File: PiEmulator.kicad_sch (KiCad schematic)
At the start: 26 parts, among them J1 Conn_01x01, J2 Conn_01x01, J3 USB_C_Receptacle_USB2.0, U1 ADA3708, U3 BQ24090DGQ

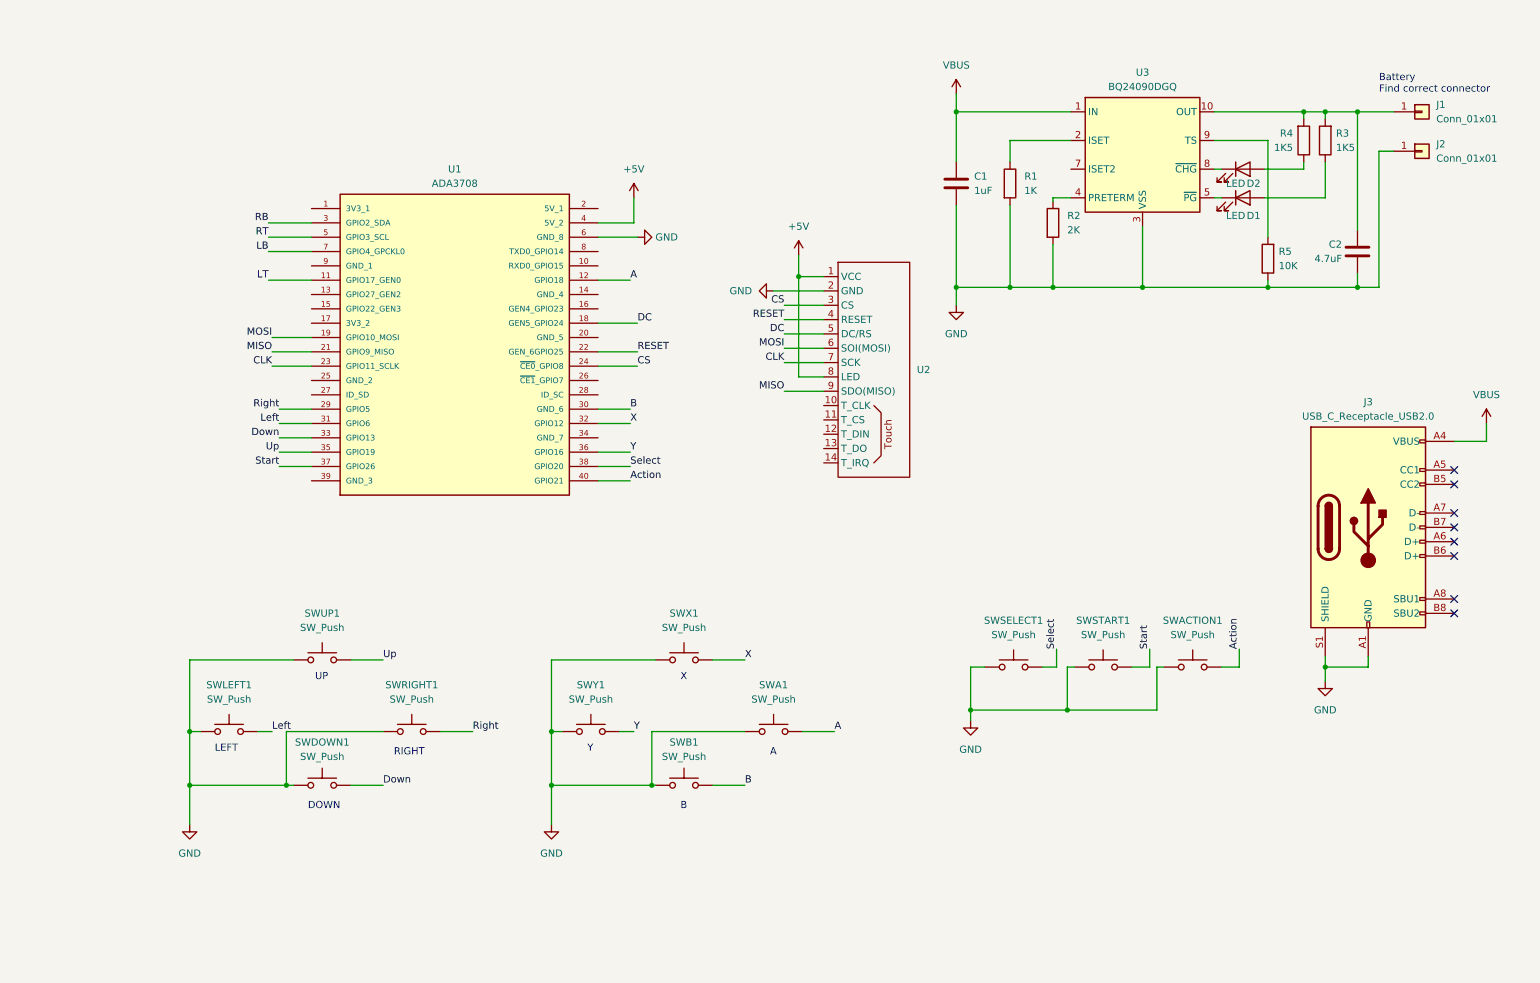
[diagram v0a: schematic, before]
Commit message: swapped buttons
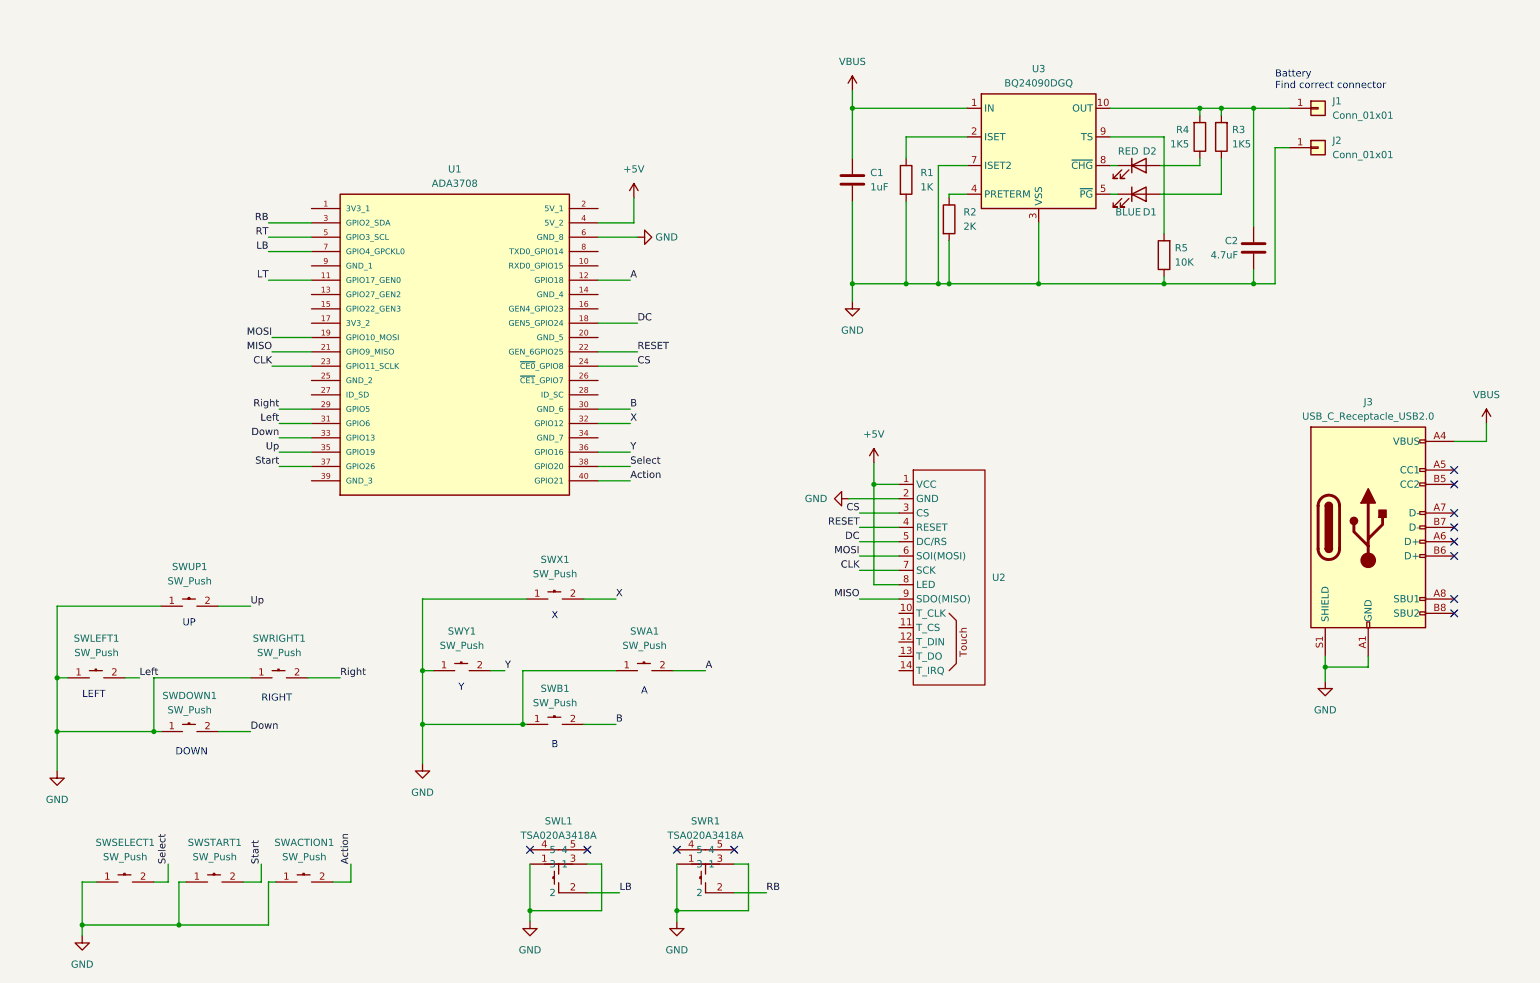
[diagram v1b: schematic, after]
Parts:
- removed SWA1, SWACTION1, SWB1, SWDOWN1, SWLEFT1, SWRIGHT1, SWSELECT1, SWSTART1, SWUP1, SWX1, SWY1: SW_Push, Button_Switch_SMD:PCB-Button, symbol Switch:SW_Push
- added SWA1, SWACTION1, SWB1, SWDOWN1, SWLEFT1, SWRIGHT1, SWSELECT1, SWSTART1, SWUP1, SWX1, SWY1: SW_Push, easyeda2kicad:SW-SMD_4P-L6.2-W6.2-P4.00-LS7.0, symbol easyeda2kicad:GT-TC063F-H025-L30
- added SWL1, SWR1: TSA020A3418A, easyeda2kicad:SW-SMD_TSA020XXXXXX, symbol easyeda2kicad:TSA020A3418A
- D1: value LED -> BLUE
- D2: value LED -> RED
- J1: footprint (none) -> Connector_Wago:SolderWirePad_4x4mm
- J2: footprint (none) -> Connector_Wire:Solder_Pad_4x4mm
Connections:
- net A: now also SWA1.2
- net Action: now also SWACTION1.2
- net B: now also SWB1.2
- net Down: now also SWDOWN1.2
- net GND: now also U3.7 (ISET2), SWA1.1, SWACTION1.1, SWB1.1, SWDOWN1.1, SWL1.1, SWL1.3, SWLEFT1.1, SWR1.1, SWR1.3, SWRIGHT1.1, SWSELECT1.1, SWSTART1.1, SWUP1.1, SWX1.1, SWY1.1
- net LB: now also SWL1.2
- net Left: now also SWLEFT1.2
- net RB: now also SWR1.2
- net Right: now also SWRIGHT1.2
- net Select: now also SWSELECT1.2
- net Start: now also SWSTART1.2
- net Up: now also SWUP1.2
- net X: now also SWX1.2
- net Y: now also SWY1.2
- no-connect marks 8 -> 12
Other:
- moved on the sheet: C1, C2, D1, D2, J1, J2, R1, R2, R3, R4, R5, U2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

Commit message: routed
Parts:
- D1, D2: footprint (none) -> LED_SMD:LED_0402_1005Metric
- R1: value 1K -> 540; footprint (none) -> Resistor_SMD:R_0603_1608Metric
- R2: footprint (none) -> Resistor_SMD:R_0603_1608Metric
- R3, R4, R5: footprint (none) -> Resistor_SMD:R_0402_1005Metric
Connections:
- net +5V is gone; now on net +BATT: U1.4 (5V_2), U2.1 (VCC), U2.8 (LED)
- net A: now also U1.32 (GPIO12); no longer U1.12 (GPIO18)
- net Action: now also U1.3 (GPIO2_SDA); no longer U1.40 (GPIO21)
- net B: now also U1.35 (GPIO19); no longer U1.30 (GND_6)
- net Down: now also U1.31 (GPIO6); no longer U1.33 (GPIO13)
- net GND: now also U1.14 (GND_4), U1.20 (GND_5), U1.25 (GND_2), U1.30 (GND_6), U1.34 (GND_7), U1.39 (GND_3), U1.9 (GND_1)
- net Left: now also U1.29 (GPIO5); no longer U1.31 (GPIO6)
- net RB: now also U1.40 (GPIO21); no longer U1.3 (GPIO2_SDA)
- net Right: now also U1.13 (GPIO27_GEN2); no longer U1.29 (GPIO5)
- net Up: now also U1.33 (GPIO13); no longer U1.35 (GPIO19)
- net X: now also U1.12 (GPIO18); no longer U1.32 (GPIO12)
- net +BATT: now reaches C2.1, J1.1 (Pin_1), R3.2, R4.2, U3.10 (OUT)
- net +BATT: now also U1.2 (5V_1)
- no-connect marks 12 -> 27
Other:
- moved on the sheet: C1, C2, D1, D2, J1, J2, R1, R2, R3, R4, R5, U1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

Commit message: silkscreen + minor fixes
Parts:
- added H1, H2, H3, H4: MountingHole, MountingHole:MountingHole_2.5mm, symbol Mechanical:MountingHole
- C1: footprint (none) -> Capacitor_SMD:C_0402_1005Metric
- C2: footprint (none) -> Capacitor_SMD:C_0603_1608Metric
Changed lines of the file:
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@@
+    )
+  )
+  (symbol (lib_id "Mechanical:MountingHole") (at 219.71 155.575 0) (unit 1)
+    (in_bom yes) (on_board yes) (dnp no)
+    (property "Reference" "H4" (at 222.25 154.305 0)
+      (effects (font (size 1.27 1.27)) (justify left))
+    )
+    (property "Value" "MountingHole" (at 222.25 156.845 0)
+      (effects (font (size 1.27 1.27)) (justify left))
+    )
+    (property "Footprint" "MountingHole:MountingHole_2.5mm" (at 219.71 155.575 0)
+      (effects (font (size 1.27 1.27)) hide)
+    )
+    (property "Datasheet" "~" (at 219.71 155.575 0)
+      (effects (font (size 1.27 1.27)) hide)
+    )
+    (instances
+      (project "PiEmulator"
+        (path "/57df2d17-e1a3-4125-a0e7-53b56f3ddd17"
+          (reference "H4") (unit 1)
+        )
+      )
     )
   )
@@
     )
   )
+  (symbol (lib_id "Mechanical:MountingHole") (at 219.71 149.86 0) (unit 1)
+    (in_bom yes) (on_board yes) (dnp no)
+    (property "Reference" "H3" (at 222.25 148.59 0)
+      (effects (font (size 1.27 1.27)) (justify left))
+    )
+    (property "Value" "MountingHole" (at 222.25 151.13 0)
+      (effects (font (size 1.27 1.27)) (justify left))
+    )
+    (property "Footprint" "MountingHole:MountingHole_2.5mm" (at 219.71 149.86 0)
+      (effects (font (size 1.27 1.27)) hide)
+    )
+    (property "Datasheet" "~" (at 219.71 149.86 0)
+      (effects (font (size 1.27 1.27)) hide)
+    )
+    (instances
+      (project "PiEmulator"
+        (path "/57df2d17-e1a3-4125-a0e7-53b56f3ddd17"
+          (reference "H3") (unit 1)
+        )
+      )
+    )
+  )
   (symbol (lib_name "GT-TC063F-H025-L30_1") (lib_id "easyeda2kicad:GT-TC063F-H025-L30") (at 37.465 179.705 0) (unit 1)
     (in_bom yes) (on_board yes) (dnp no) (fields_autoplaced)
@@
       (effects (font (size 1.27 1.27)) (justify left))
     )
-    (property "Footprint" "" (at 167.3352 57.15 0)
+    (property "Footprint" "Capacitor_SMD:C_0402_1005Metric" (at 167.3352 57.15 0)
       (effects (font (size 1.27 1.27)) hide)
     )
@@
       (effects (font (size 1.27 1.27)) (justify right))
     )
-    (property "Footprint" "" (at 236.5248 69.215 0)
+    (property "Footprint" "Capacitor_SMD:C_0603_1608Metric" (at 236.5248 69.215 0)
       (effects (font (size 1.27 1.27)) hide)
     )
@@
     )
   )
+  (symbol (lib_id "Mechanical:MountingHole") (at 213.995 155.575 0) (mirror y) (unit 1)
+    (in_bom yes) (on_board yes) (dnp no) (fields_autoplaced)
+    (property "Reference" "H2" (at 211.455 154.305 0)
+      (effects (font (size 1.27 1.27)) (justify left))
+    )
+    (property "Value" "MountingHole" (at 211.455 156.845 0)
+      (effects (font (size 1.27 1.27)) (justify left))
+    )
+    (property "Footprint" "MountingHole:MountingHole_2.5mm" (at 213.995 155.575 0)
+      (effects (font (size 1.27 1.27)) hide)
+    )
+    (property "Datasheet" "~" (at 213.995 155.575 0)
+      (effects (font (size 1.27 1.27)) hide)
+    )
+    (instances
+      (project "PiEmulator"
+        (path "/57df2d17-e1a3-4125-a0e7-53b56f3ddd17"
+          (reference "H2") (unit 1)
+        )
+      )
+    )
+  )
   (symbol (lib_id "Device:R") (at 175.895 53.34 0) (unit 1)
     (in_bom yes) (on_board yes) (dnp no) (fields_autoplaced)
@@
         )
       )
+    )
+  )
+  (symbol (lib_id "Mechanical:MountingHole") (at 213.995 149.86 0) (mirror y) (unit 1)
+    (in_bom yes) (on_board yes) (dnp no) (fields_autoplaced)
+    (property "Reference" "H1" (at 211.455 148.59 0)
+      (effects (font (size 1.27 1.27)) (justify left))
+    )
+    (property "Value" "MountingHole" (at 211.455 151.13 0)
+      (effects (font (size 1.27 1.27)) (justify left))
+    )
+    (property "Footprint" "MountingHole:MountingHole_2.5mm" (at 213.995 149.86 0)
+      (effects (font (size 1.27 1.27)) hide)
+    )
+    (property "Datasheet" "~" (at 213.995 149.86 0)
+      (effects (font (size 1.27 1.27)) hide)
+    )
+    (instances
+      (project "PiEmulator"
+        (path "/57df2d17-e1a3-4125-a0e7-53b56f3ddd17"
+          (reference "H1") (unit 1)
+        )
+      )

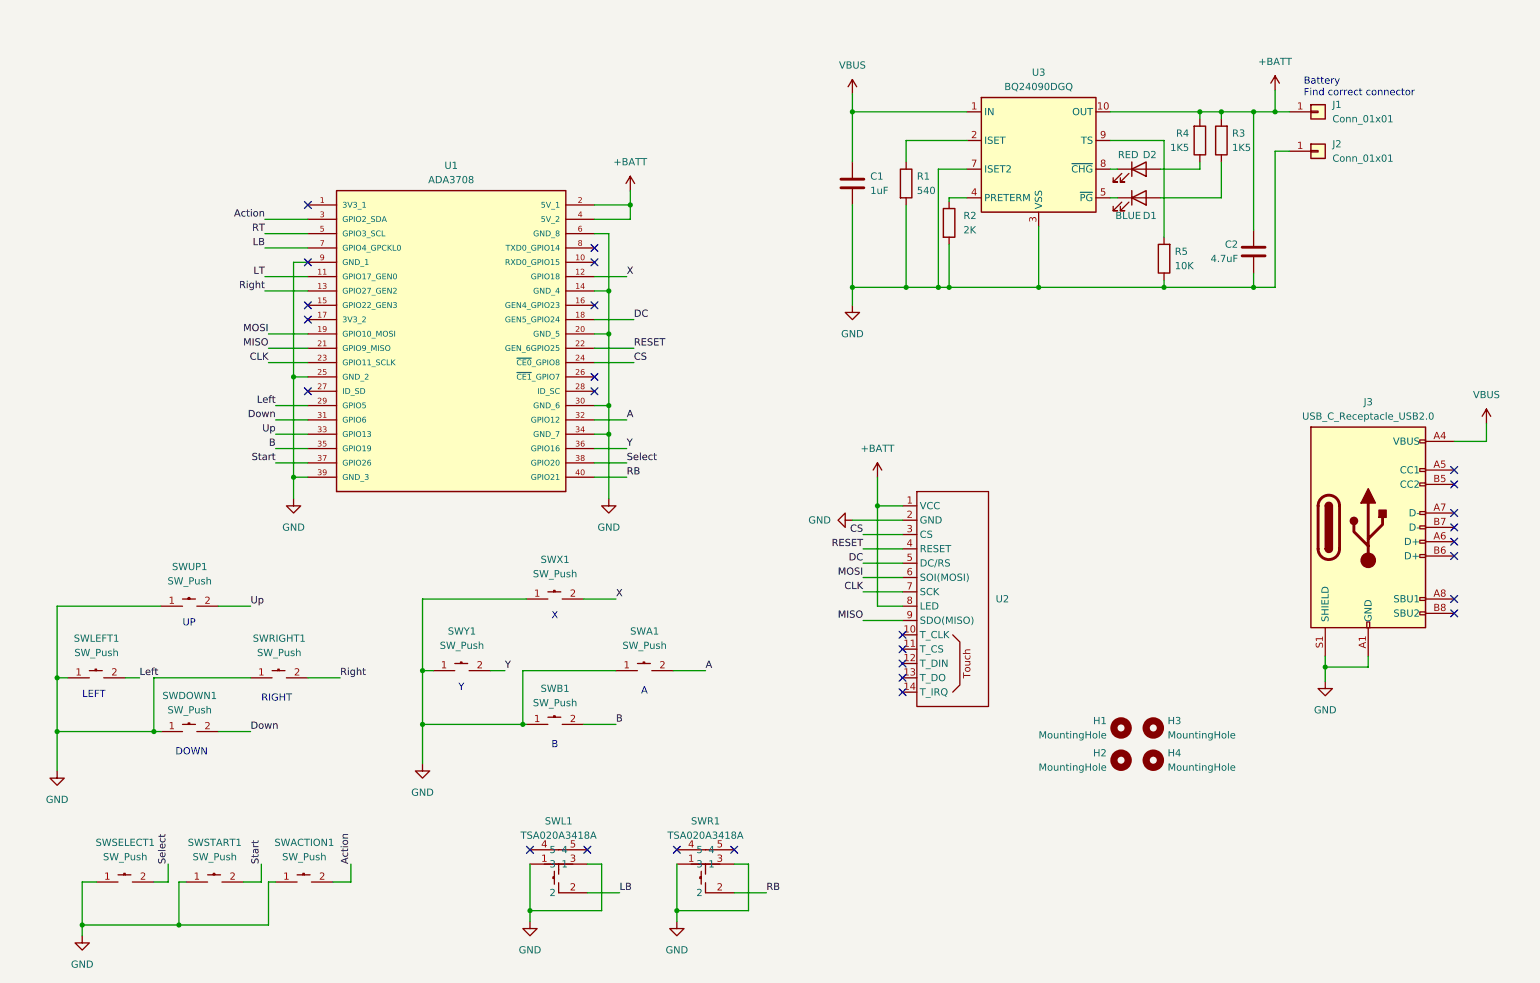
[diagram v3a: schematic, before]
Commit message: added boost convertor
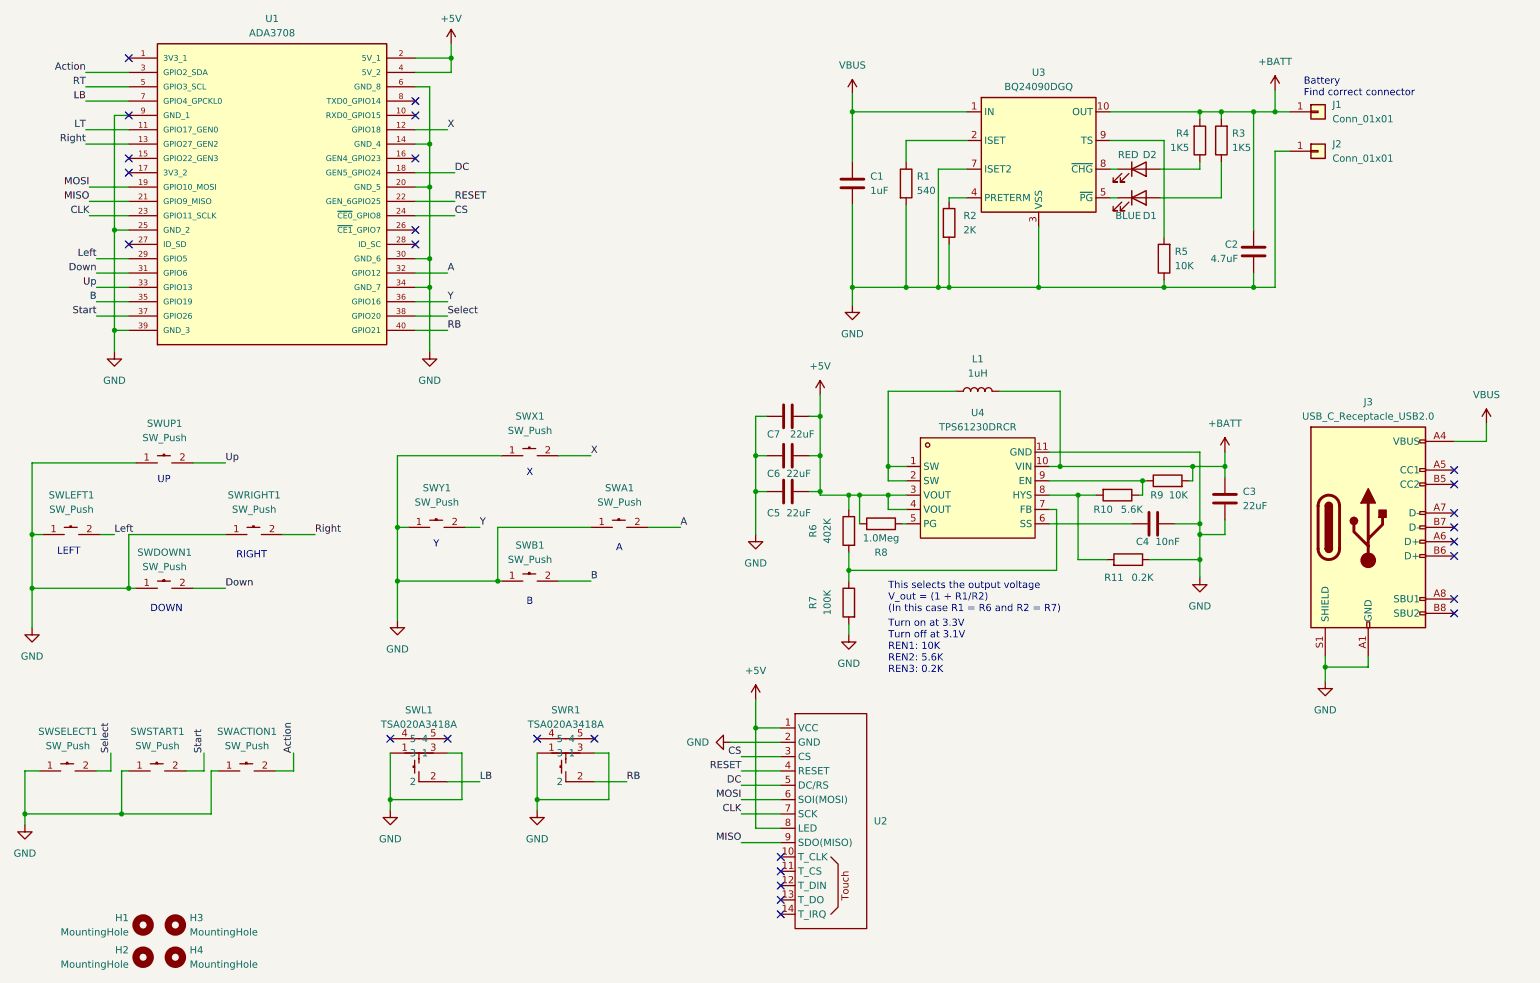
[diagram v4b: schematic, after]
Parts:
- added C3, C5, C6, C7: 22uF, Capacitor_SMD:C_0805_2012Metric, symbol Device:C
- added C4: 10nF, Capacitor_SMD:C_0402_1005Metric, symbol Device:C
- added L1: 1uH, Inductor_SMD:L_0603_1608Metric, symbol Device:L
- added R10: 5.6K, Resistor_SMD:R_0603_1608Metric, symbol Device:R
- added R11: 0.2K, Resistor_SMD:R_0603_1608Metric, symbol Device:R
- added R6: 402K, Resistor_SMD:R_0603_1608Metric, symbol Device:R
- added R7: 100K, Resistor_SMD:R_0603_1608Metric, symbol Device:R
- added R8: 1.0Meg, Resistor_SMD:R_0603_1608Metric, symbol Device:R
- added R9: 10K, Resistor_SMD:R_0402_1005Metric, symbol Device:R
- added U4: TPS61230DRCR, easyeda2kicad:VSON-10_L3.0-W3.0-P0.50-TL-EP_TPS61230DRCR, symbol easyeda2kicad:TPS61230DRCR
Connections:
- net +BATT: now also C3.1, L1.2, R9.2, U4.10 (VIN); no longer U1.2 (5V_1), U1.4 (5V_2), U2.1 (VCC), U2.8 (LED)
- net GND: now also C3.2, C4.2, C5.1, C6.1, C7.1, R11.1, R7.2, U4.11 (GND)
- new net: R8.1, U4.5 (PG)
- new net: R10.2, R11.2, U4.8 (HYS)
- new net: L1.1, U4.1 (SW), U4.2 (SW)
- new net: C4.1, U4.6 (SS)
- new net: R6.2, R7.1, U4.7 (FB)
- new net: R10.1, R9.1, U4.9 (EN)
- new net +5V: C5.2, C6.2, C7.2, R6.1, R8.2, U1.2 (5V_1), U1.4 (5V_2), U2.1 (VCC), U2.8 (LED), U4.3 (VOUT), U4.4 (VOUT)
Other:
- note added: "This selects the output voltage V_out = (1 + R1/R2) (In this case R1 = R6 and R2 = R7)"
- note added: "Turn on at 3.3V Turn off at 3.1V REN1: 10K REN2: 5.6K REN3: 0.2K"
- moved on the sheet: H1, H2, H3, H4, SWA1, SWACTION1, SWB1, SWDOWN1, SWL1, SWLEFT1, SWR1, SWRIGHT1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
